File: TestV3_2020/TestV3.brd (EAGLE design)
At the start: 160 x 100 mm, 57 parts, among them J3 USB_B_PTH, Q1 NPN-BJT, Q2 NPN-BJT, U2 MP2451

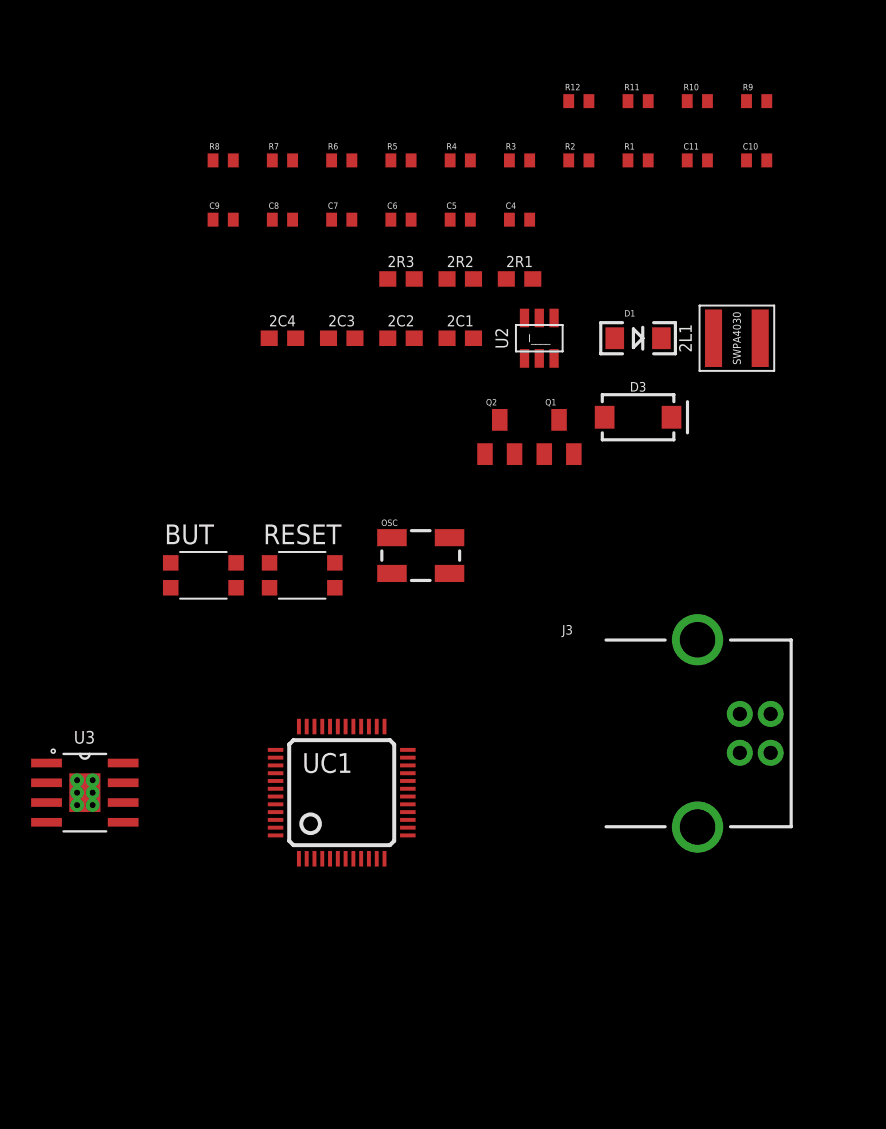
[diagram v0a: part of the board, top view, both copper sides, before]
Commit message: Added Datasheets folder and cleaned up the schematic to use less random libraries
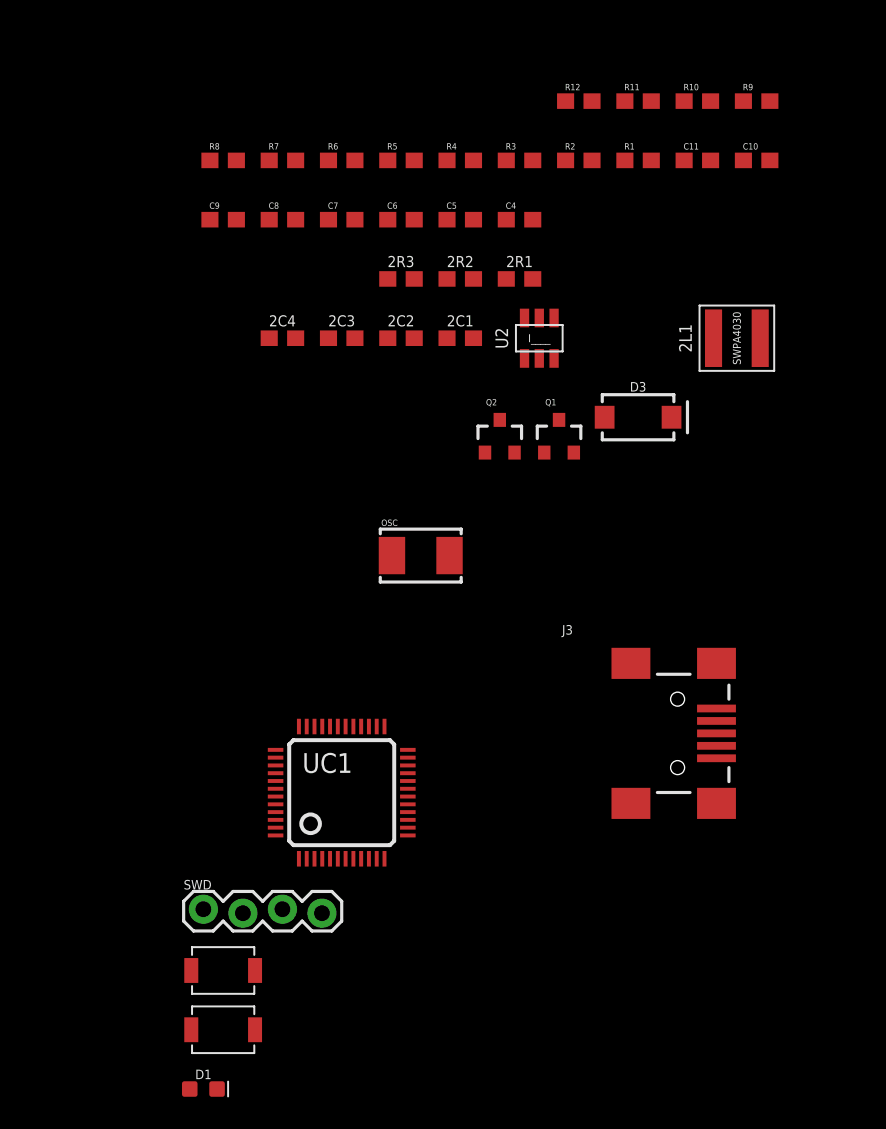
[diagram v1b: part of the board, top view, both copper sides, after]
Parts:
- removed BUT, RESET: KMR211GLFS, okie:PUSHBUTTON-KMR241GLFS
- removed U3: (no value), JH:POWERPAD-SOIC-8
- added S1, S2: 34-MOMENTARY-SWITCH, JH:3*4-MOMENTARY-SWITCH
- added SWD: (no value), SparkFun-Connectors:1X04_LOCK
- 2C11, 2C12: value 22UF -> 47uF
- C10, C11, C4, C5, C6, C7: device SparkFun:C0402 -> JH:C0603
- C8, C9: value 18pF -> 20pF; device SparkFun:C0402 -> JH:C0603
- D1: value Blue -> BLUE; device SparkFun:LED-1206 -> SparkFun-LED:LED-0603
- D2, D3: value 2D1 -> SS34
- J3: value USB_B_PTH -> USB_MINI-B_SMT; device SparkFun-Connectors:USB-B-PTH -> SparkFun-Connectors:USB-MINIB
- OSC: device SparkFun2:CRYSTAL-SMD-5X3 -> SparkFun-Clocks:CRYSTAL-SMD-5X3.2-2PAD
- Q1, Q2: value NPN-BJT -> 600mA/40V; device SparkFun2:SOT23 -> SparkFun-DiscreteSemi:SOT23-3
- R1, R10, R11, R12, R2, R3, R4, R5, R6, R7, R8, R9: device SparkFun:C0402 -> JH:R0603
- R15: value 10.2 -> 10k
- UC1: device stm32:LQFP48 -> JH:LQFP48
- moved D1 55.8 mm to (-50.8, -14.0)
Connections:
- net AV- renamed AGND
- removed net VIN: U3.7
- net 21: now also SWD.2
- net 22: now also SWD.3
- net 32: now also S1.P2; no longer BUT.P$2, BUT.P$4
- net GND: now also SWD.1; no longer U3.6, U3.9, U3.P$1, U3.P$2, U3.P$3, U3.P$4, U3.P$5, U3.P$6
- net N$1: now also S1.P1; no longer BUT.P$1, BUT.P$3
- net N$4: now also S2.P1; no longer RESET.P$1, RESET.P$3
- net OSC_IN: now also OSC.P$2; no longer OSC.3
- net OSC_OUT: now also OSC.P$1; no longer OSC.1
- net RESET: now also S2.P2; no longer RESET.P$2, RESET.P$4
- net VCC: now also SWD.4

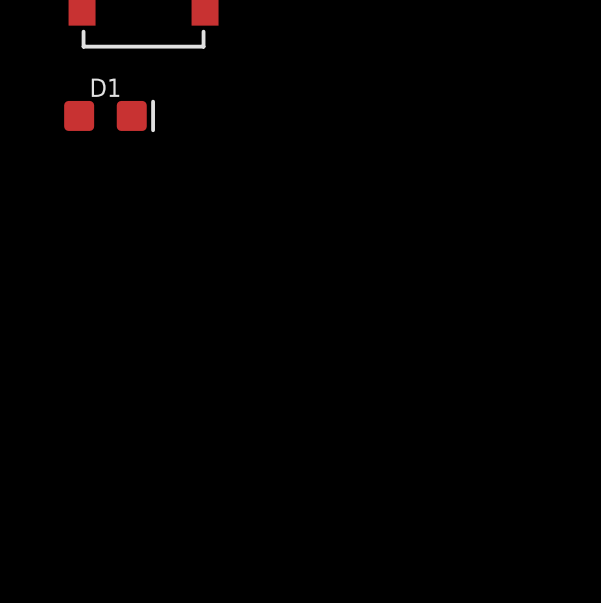
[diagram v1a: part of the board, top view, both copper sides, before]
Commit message: Small changes to STM32: Added protection diodes between V_USB and VCC, and added ferrite beads to filter analog voltage
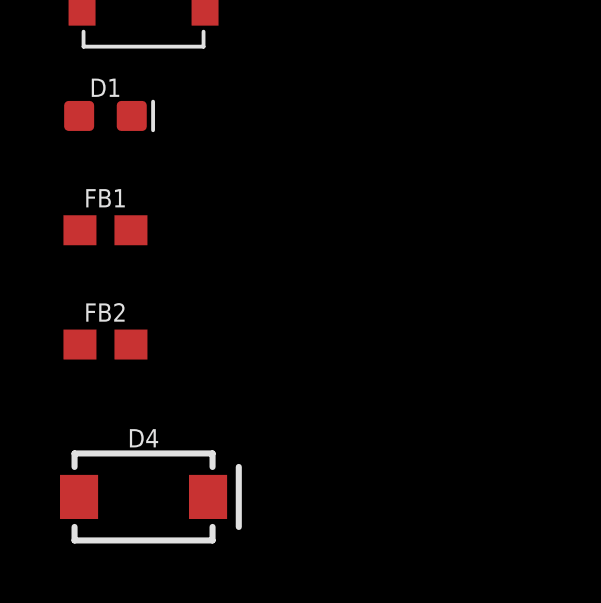
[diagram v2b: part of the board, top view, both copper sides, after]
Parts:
- added D4: 3A/40V/500mV, SparkFun-DiscreteSemi:SMA-DIODE
- added FB1, FB2: 30Ω/1.8A, SparkFun-Coils:0603
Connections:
- net 12V: now also D4.C
- net AGND: now also FB2.2
- net GND: now also FB2.1
- net VCC: now also FB1.1
- net VCCA: now also FB1.2
- net V_USB: now also D4.A
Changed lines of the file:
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@@
 <drawing>
 <settings>
-<setting alwaysvectorfont="yes"/>
+<setting alwaysvectorfont="no"/>
 <setting verticaltext="up"/>
 </settings>
@@
 <attribute name="VALUE" x="-50.8" y="-14.605" size="0.6096" layer="27" font="vector" ratio="20" align="top-center"/>
 </element>
+<element name="FB1" library="SparkFun-Coils" library_urn="urn:adsk.eagle:library:512" package="0603" package3d_urn="urn:adsk.eagle:package:37574/1" value="30Ω/1.8A" x="-50.8" y="-17.78" smashed="yes">
+<attribute name="NAME" x="-50.8" y="-17.018" size="0.6096" layer="25" font="vector" ratio="20" align="bottom-center"/>
+<attribute name="PROD_ID" value="NDUC-07859" x="-50.8" y="-17.78" size="1.778" layer="27" display="off"/>
+<attribute name="VALUE" x="-50.8" y="-18.542" size="0.6096" layer="27" font="vector" ratio="20" align="top-center"/>
+</element>
+<element name="FB2" library="SparkFun-Coils" library_urn="urn:adsk.eagle:library:512" package="0603" package3d_urn="urn:adsk.eagle:package:37574/1" value="30Ω/1.8A" x="-50.8" y="-21.59" smashed="yes">
+<attribute name="NAME" x="-50.8" y="-20.828" size="0.6096" layer="25" font="vector" ratio="20" align="bottom-center"/>
+<attribute name="PROD_ID" value="NDUC-07859" x="-50.8" y="-21.59" size="1.778" layer="27" display="off"/>
+<attribute name="VALUE" x="-50.8" y="-22.352" size="0.6096" layer="27" font="vector" ratio="20" align="top-center"/>
+</element>
+<element name="D4" library="SparkFun-DiscreteSemi" library_urn="urn:adsk.eagle:library:514" package="SMA-DIODE" package3d_urn="urn:adsk.eagle:package:38443/1" value="3A/40V/500mV" x="-49.53" y="-26.67" smashed="yes">
+<attribute name="NAME" x="-49.53" y="-25.019" size="0.6096" layer="25" font="vector" ratio="20" align="bottom-center"/>
+<attribute name="PROD_ID" value="DIO-09886" x="-49.53" y="-26.67" size="1.778" layer="27" display="off"/>
+<attribute name="VALUE" x="-49.53" y="-28.321" size="0.6096" layer="27" font="vector" ratio="20" align="top-center"/>
+</element>
 </elements>
 <signals>
@@
 <contactref element="R2" pad="2"/>
 <contactref element="SWD" pad="4"/>
-<wire x1="-43.18" y1="-2.667" x2="-46.16" y2="2.33" width="0" layer="19" extent="1-1"/>
+<contactref element="FB1" pad="1"/>
+<wire x1="-43.18" y1="-2.667" x2="-51.65" y2="-17.78" width="0" layer="19" extent="1-1"/>
+<wire x1="-46.16" y1="2.33" x2="-43.18" y2="-2.667" width="0" layer="19" extent="1-1"/>
 <wire x1="-44.66" y1="9.33" x2="-46.16" y2="2.33" width="0" layer="19" extent="1-1"/>
 <wire x1="-37.66" y1="7.83" x2="-44.66" y2="9.33" width="0" layer="19" extent="1-1"/>
@@
 <contactref element="SWD" pad="1"/>
 <contactref element="D1" pad="C"/>
+<contactref element="FB2" pad="1"/>
+<wire x1="-49.923" y1="-13.97" x2="-51.65" y2="-21.59" width="0" layer="19" extent="1-1"/>
 <wire x1="-50.8" y1="-2.413" x2="-49.923" y2="-13.97" width="0" layer="19" extent="1-1"/>
 <wire x1="-46.16" y1="2.83" x2="-50.8" y2="-2.413" width="0" layer="19" extent="1-1"/>
@@
 <contactref element="C4" pad="1"/>
 <contactref element="UC1" pad="9"/>
+<contactref element="FB1" pad="2"/>
+<wire x1="-40.66" y1="0.83" x2="-49.95" y2="-17.78" width="0" layer="19" extent="1-1"/>
 <wire x1="-31.33" y1="41.91" x2="-40.66" y2="0.83" width="0" layer="19" extent="1-1"/>
 </signal>
@@
 <contactref element="R8" pad="2"/>
 <contactref element="J3" pad="VBUS"/>
+<contactref element="D4" pad="A"/>
+<wire x1="-17.82" y1="10.49" x2="-51.68" y2="-26.67" width="0" layer="19" extent="1-1"/>
 <wire x1="-48.68" y1="45.72" x2="-17.82" y2="10.49" width="0" layer="19" extent="1-1"/>
 </signal>
@@
 <contactref element="U1" pad="2"/>
 <contactref element="R14" pad="2"/>
-<wire x1="25.4" y1="21.17" x2="29.21" y2="24.915" width="0" layer="19" extent="1-1"/>
-<wire x1="22.44" y1="17.78" x2="25.4" y2="21.17" width="0" layer="19" extent="1-1"/>
+<contactref element="D4" pad="C"/>
+<wire x1="-35.14" y1="34.29" x2="-47.38" y2="-26.67" width="0" layer="19" extent="1-1"/>
+<wire x1="-29.21" y1="35.59" x2="-35.14" y2="34.29" width="0" layer="19" extent="1-1"/>
+<wire x1="17.8562" y1="22.225" x2="-29.21" y2="35.59" width="0" layer="19" extent="1-1"/>
+<wire x1="22.44" y1="17.78" x2="17.8562" y2="22.225" width="0" layer="19" extent="1-1"/>
 <wire x1="21.17" y1="15.24" x2="22.44" y2="17.78" width="0" layer="19" extent="1-1"/>
 <wire x1="24.98" y1="15.24" x2="22.44" y2="17.78" width="0" layer="19" extent="1-1"/>
-<wire x1="17.8562" y1="22.225" x2="22.44" y2="17.78" width="0" layer="19" extent="1-1"/>
-<wire x1="-29.21" y1="35.59" x2="17.8562" y2="22.225" width="0" layer="19" extent="1-1"/>
-<wire x1="-35.14" y1="34.29" x2="-29.21" y2="35.59" width="0" layer="19" extent="1-1"/>
+<wire x1="25.4" y1="21.17" x2="22.44" y2="17.78" width="0" layer="19" extent="1-1"/>
+<wire x1="29.21" y1="24.915" x2="25.4" y2="21.17" width="0" layer="19" extent="1-1"/>
 </signal>
 <signal name="N$5">
@@
 <contactref element="UC1" pad="8"/>
 <contactref element="C4" pad="2"/>
+<contactref element="FB2" pad="2"/>
+<wire x1="-41.16" y1="0.83" x2="-49.95" y2="-21.59" width="0" layer="19" extent="1-1"/>
 <wire x1="-29.63" y1="41.91" x2="-41.16" y2="0.83" width="0" layer="19" extent="1-1"/>
 </signal>

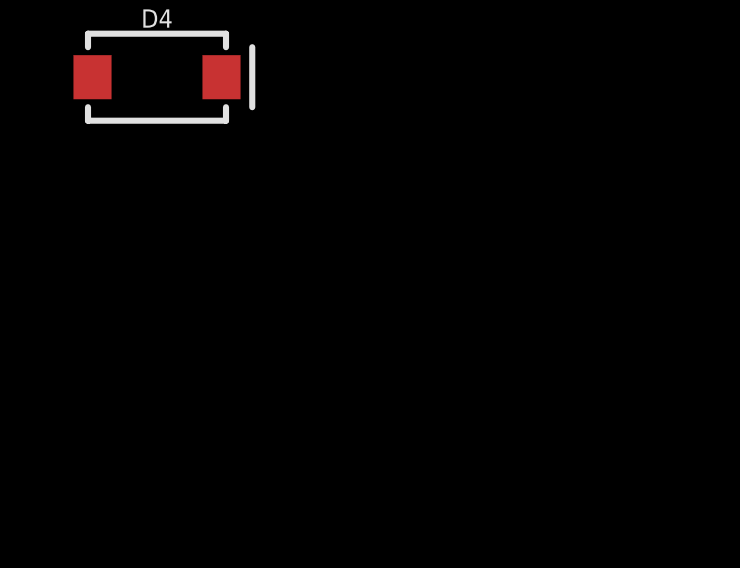
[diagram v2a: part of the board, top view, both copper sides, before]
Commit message: IDK what I did but added datasheet of INA20x current shunt controller cuz will be using that
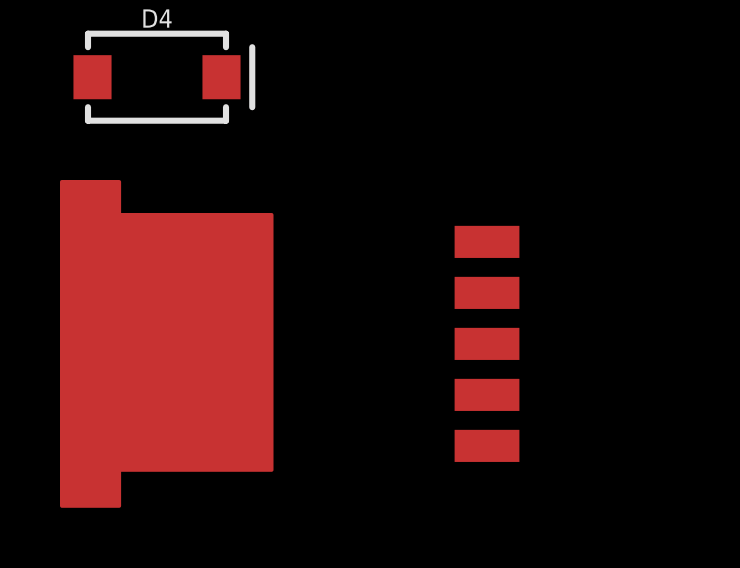
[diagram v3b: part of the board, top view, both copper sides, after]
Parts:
- added U3: LM2587, JH:TO-263
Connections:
- new net VIN: U3.P5
- net GND: now also U3.P3
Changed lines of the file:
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@@
 <drawing>
 <settings>
-<setting alwaysvectorfont="no"/>
+<setting alwaysvectorfont="yes"/>
 <setting verticaltext="up"/>
 </settings>
@@
 <attribute name="VALUE" x="-49.53" y="-28.321" size="0.6096" layer="27" font="vector" ratio="20" align="top-center"/>
 </element>
+<element name="U3" library="JH" library_urn="urn:adsk.eagle:library:6027132" package="TO-263" package3d_urn="urn:adsk.eagle:package:9157861/2" value="LM2587" x="-49.53" y="-35.56" smashed="yes"/>
 </elements>
 <signals>
@@
 <contactref element="D1" pad="C"/>
 <contactref element="FB2" pad="1"/>
+<contactref element="U3" pad="P3"/>
+<wire x1="-51.65" y1="-21.59" x2="-38.53" y2="-35.56" width="0" layer="19" extent="1-1"/>
 <wire x1="-49.923" y1="-13.97" x2="-51.65" y2="-21.59" width="0" layer="19" extent="1-1"/>
 <wire x1="-50.8" y1="-2.413" x2="-49.923" y2="-13.97" width="0" layer="19" extent="1-1"/>
@@
 <wire x1="-29.63" y1="41.91" x2="-41.16" y2="0.83" width="0" layer="19" extent="1-1"/>
 </signal>
+<signal name="VIN">
+<contactref element="U3" pad="P5"/>
+</signal>
 </signals>

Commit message: Finally finished LM2587 Boost Circuit, together with INA169+LM393 overcurrent protection
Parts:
- added 3C1: 100uF, SparkFun-Capacitors:PANASONIC_D
- added 3C2, C12: 1uF, JH:C0603
- added 3C3, 3C5: 0.1uF, JH:C0603
- added 3C4: 1000uF, JH:1000UF-CAP
- added 3D1: SS510, diode:SMB
- added 3L1: 56uH, JH:CDRH127
- added 3R1: 2.94k, JH:R0603
- added 3R2: 1.5k, JH:R0603
- added 3U1: LM2587, JH:TO-263
- added C3: 100uF, SparkFun-Capacitors:NIC_10X10.5_CAP
- added D5: SS34, SparkFun-DiscreteSemi:SMA-DIODE
- added J1: (no value), SparkFun-Connectors:1X03_LOCK
- added POT1, POT2: 10k, JH:3296-TRIMPOT
- added R18: 45k, JH:R0603
- added R19: 0.15, SparkFun-Resistors:0805
- added R20: 3k, JH:R0603
- added R21: 10k, JH:R0603
- added U$6: LM393, JH:SOIC-8
- added U4: INA169, SparkFun-IC-Special-Function:SOT23-5
- J3: value USB_MINI-B_SMT -> (none); device SparkFun-Connectors:USB-MINIB -> SparkFun-Connectors:USB-B-MICRO-SMD
- U3: value LM2587 -> 10k; device JH:TO-263 -> JH:SOIC-8
- moved U3 38.9 mm to (-57.1, -73.7)
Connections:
- removed net VIN: U3.P5
- new net FDBK: 3R2.2, 3U1.P2, D5.C, POT1.1, POT1.2
- new net N$14: 3C4.+, 3D1.C, C3.+, R18.2, R19.1, U4.3
- new net N$16: POT1.3, U3.5, U3.6
- new net N$17: R21.2, U$6.3, U4.1
- new net N$18: R18.1, U3.7
- new net N$19: D5.A, R20.1, U$6.1
- new net N$20: POT2.2, U$6.2
- new net N$22: J1.1, U3.3
- new net N$23: J1.2, U3.2
- new net N$24: J1.3, U3.1
- new net N$34: 3D1.A, 3L1.2, 3U1.P4
- new net N$36: 3R1.2, 3U1.P1
- new net N$37: 3C2.1, 3R1.1
- new net VCC_2: R19.2, U4.4
- net 12V: now also 3C1.+, 3C5.1, 3L1.1, 3U1.P5, U4.5
- net 3.3V: now also 3C3.1, C12.1, POT2.1, R20.2, U$6.8, U3.8
- net GND: now also 3C1.-, 3C2.2, 3C3.2, 3C4.-, 3C5.2, 3R2.1, 3U1.P$1, 3U1.P$10, 3U1.P$11, 3U1.P$12, 3U1.P$13, 3U1.P$14, 3U1.P$15, 3U1.P$16, 3U1.P$17, 3U1.P$18, 3U1.P$19, 3U1.P$2, 3U1.P$20, 3U1.P$3, 3U1.P$4, 3U1.P$5, 3U1.P$6, 3U1.P$7, 3U1.P$8, 3U1.P$9, 3U1.P3, 3U1.TAB, C12.2, C3.-, POT2.3, R21.1, U$6.4, U3.4, U4.2; no longer U3.P3

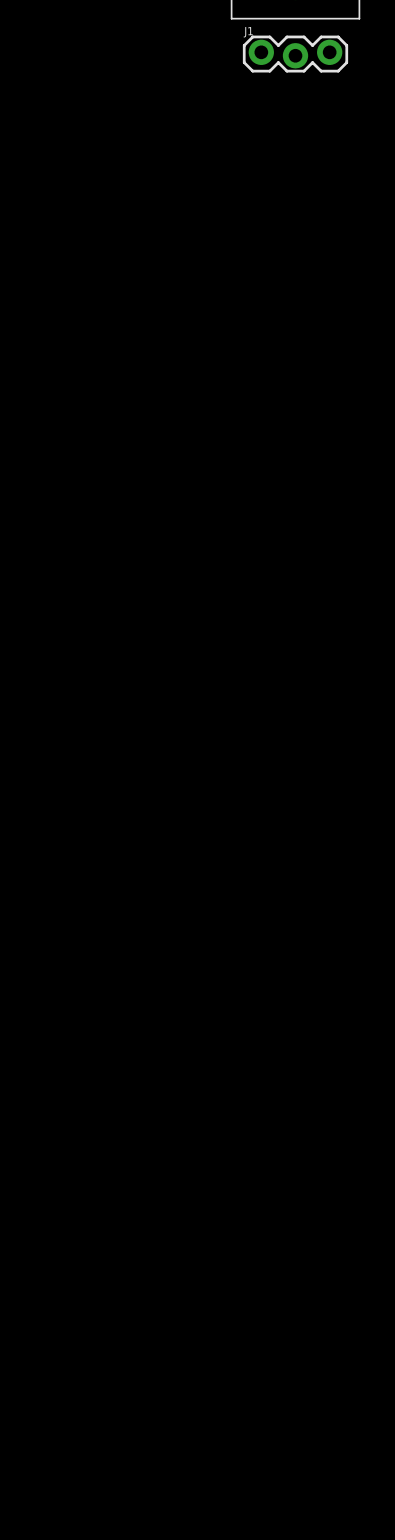
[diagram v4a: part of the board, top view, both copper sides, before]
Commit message: Finished low battery detection, motor driver and TCS3200 color sensor.
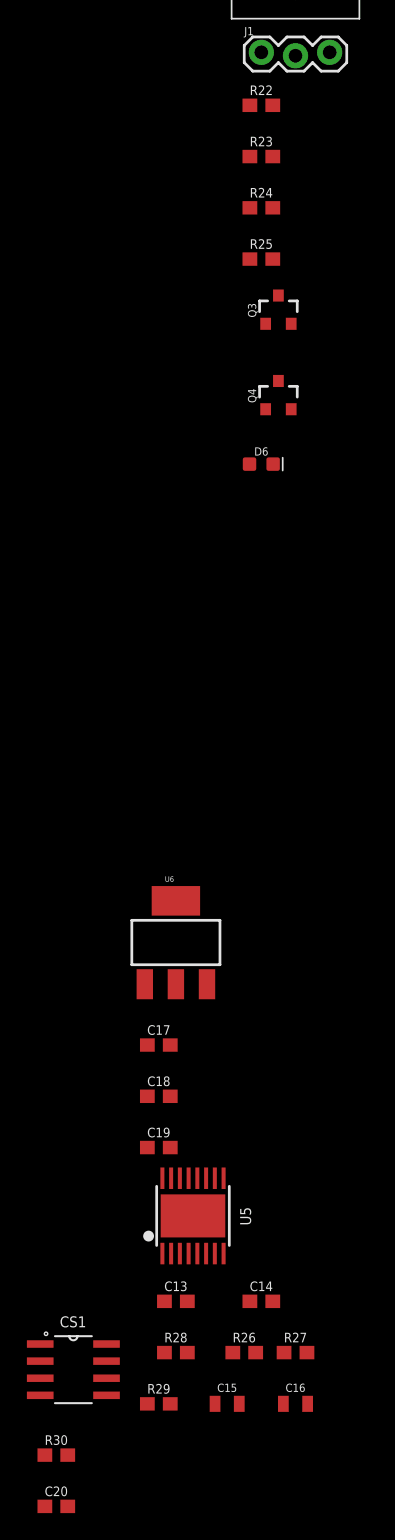
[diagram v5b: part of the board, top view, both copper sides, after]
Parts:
- added C13: 2.2uF/6.3V, JH:C0603
- added C14: 10nF/16V, JH:C0603
- added C15, C16: 10uF/16V, JH:C0805
- added C17, C18: 1uF, JH:C0603
- added C19: 4.7uF, JH:C0603
- added C20: 0.1uF, JH:C0603
- added CS1: TCS3200, JH:SOIC-8
- added D6: BLUE, SparkFun-LED:LED-0603
- added Q3, Q4: 600mA/40V, SparkFun-DiscreteSemi:SOT23-3
- added R22: 3.6k, JH:R0603
- added R23: 75k, JH:R0603
- added R24, R29: 100k, JH:R0603
- added R25: 560, JH:R0603
- added R26, R27: 0.2, JH:R0603
- added R28: 20k-75k, JH:R0603
- added R30: 10k, JH:R0603
- added U5: (no value), JH:SSOP16
- added U6: (no value), SparkFun-IC-Power:SOT223
- 2C11, 2C12: value 47uF -> 47uF/6.3v
- D4: value 3A/40V/500mV -> SS34
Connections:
- new net N$21: Q3.3, Q4.1, R24.1
- new net N$25: D6.A, R25.2
- new net N$26: D6.C, Q4.3
- new net N$27: U5.16
- new net N$28: Q3.1, R22.2, R23.1
- new net N$29: U5.15
- new net N$30: U5.9
- new net N$31: U5.10
- new net N$32: R28.1, U5.1
- new net N$33: R29.1, U5.8
- new net N$35: R26.2, U5.6
- new net N$38: R27.2, U5.3
- new net N$39: U5.2
- new net N$40: U5.4
- new net N$41: U5.7
- new net N$42: U5.5
- new net N$43: C14.1, U5.11
- new net N$44: C13.1, U5.14
- new net N$45: CS1.1
- new net N$46: CS1.2
- new net N$47: CS1.7
- new net N$48: CS1.8
- new net N$49: CS1.6
- new net N$50: CS1.3, R30.2
- new net VCC_1: C14.2, C15.1, C16.1, R28.2, R29.2, U5.12
- net 12V: now also C19.1, R23.2, R24.2, R25.1, U6.3
- net 3.3V: now also C20.2, CS1.5
- net AGND: now also C18.2
- net GND: now also C13.2, C15.2, C16.2, C17.2, C19.2, C20.1, CS1.4, Q3.2, Q4.2, R22.1, R26.1, R27.1, R30.1, U5.13, U5.PPAD, U6.1
- net VCC: now also C17.1, U6.2, U6.4
- net VCCA: now also C18.1
